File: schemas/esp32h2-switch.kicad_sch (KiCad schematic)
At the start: 37 parts, among them J1 Screw_Terminal_01x02, J2 Conn_01x15, J3 Screw_Terminal_01x02, K1 SPDT, 5V 72R, 10A 250VAC, Q1 NPN, 40V, 500mA, T1 1:1 330uH / 15uH, U1 LM1117MP-3.3, U2 LNK306P, U3 PC817

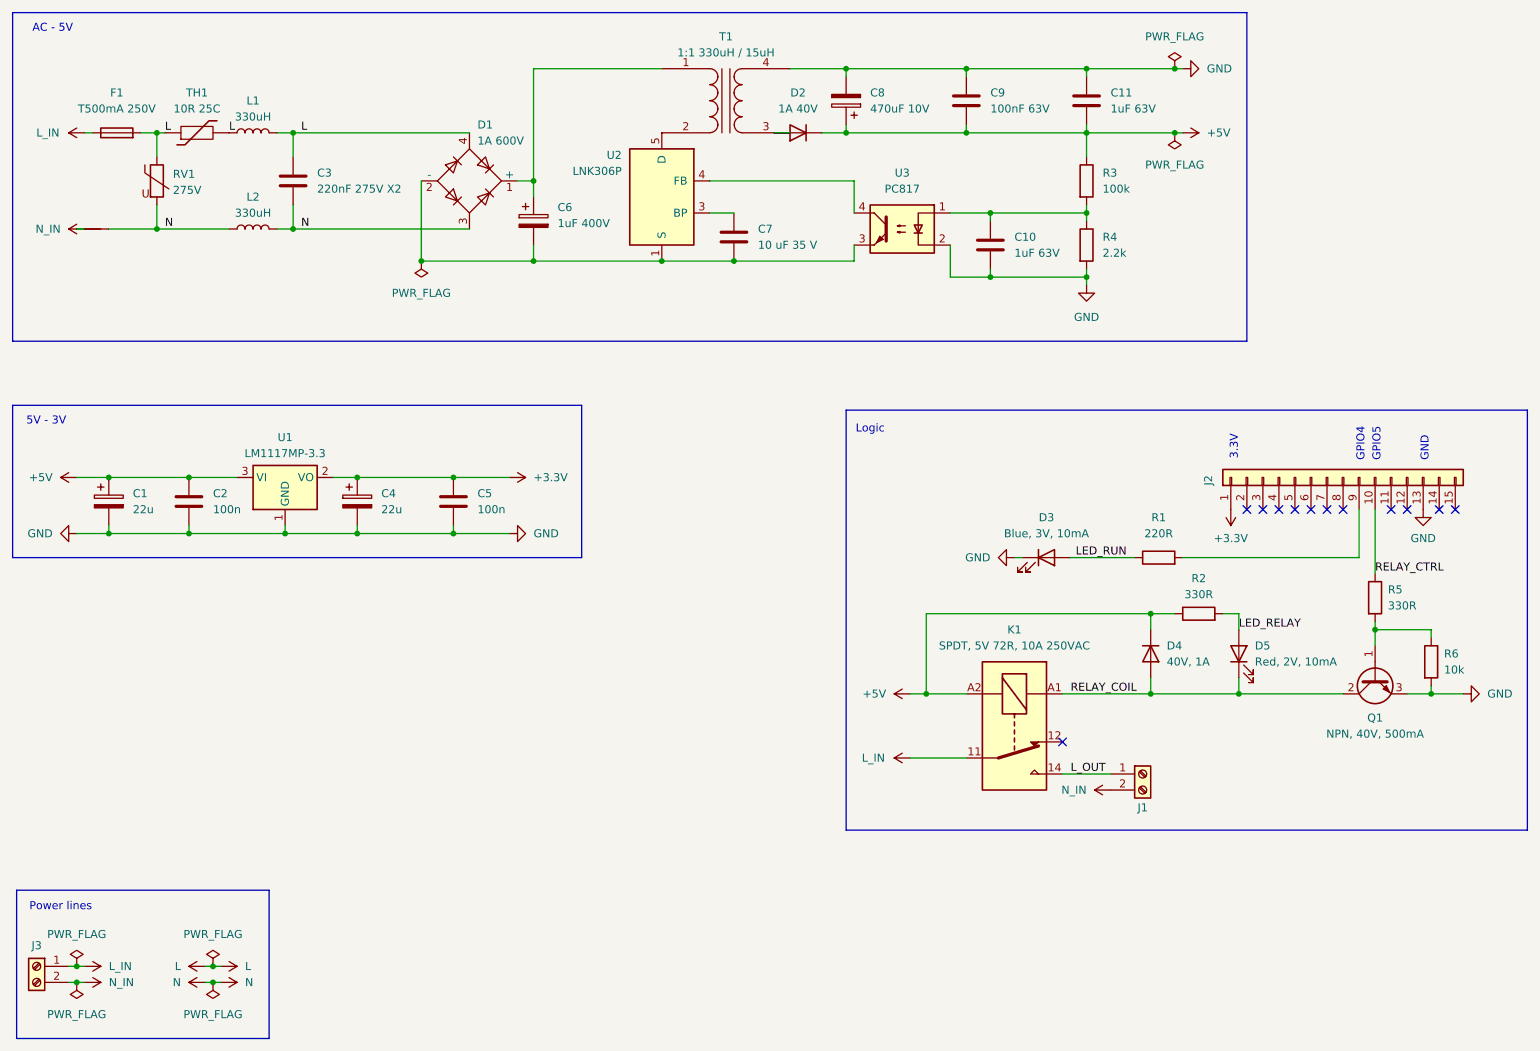
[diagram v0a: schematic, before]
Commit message: Improve layout a lot
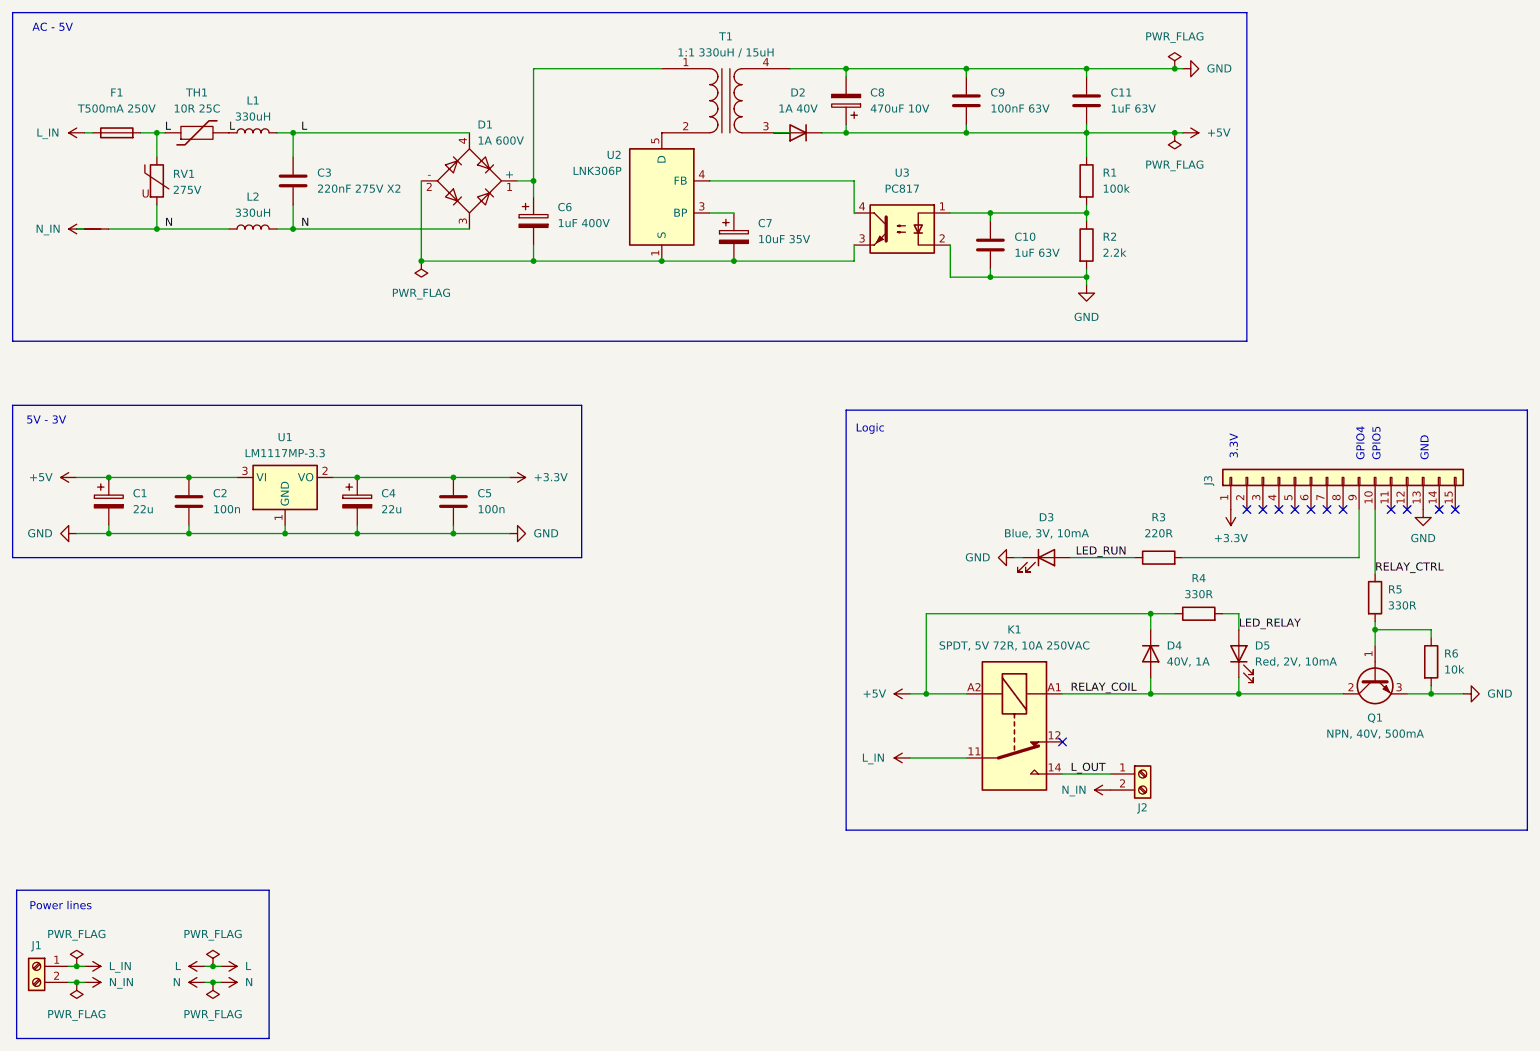
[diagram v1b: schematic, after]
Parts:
- removed C7: 10 uF 35 V, symbol Device:C
- added C7: 10uF 35V, Capacitor_THT:CP_Radial_Tantal_D6.0mm_P2.50mm, symbol Device:C_Polarized
- C10, C11: footprint (none) -> Capacitor_THT:C_Disc_D4.3mm_W1.9mm_P5.00mm
- C3: footprint (none) -> Capacitor_THT:C_Rect_L26.5mm_W5.0mm_P22.50mm_MKS4
- C6, C8: footprint (none) -> Capacitor_THT:CP_Radial_D6.3mm_P2.50mm
- C9: footprint (none) -> Capacitor_THT:C_Disc_D6.0mm_W2.5mm_P5.00mm
- D2: footprint (none) -> Diode_THT:D_DO-41_SOD81_P10.16mm_Horizontal
- J2: renamed from J1; footprint TerminalBlock_Phoenix:TerminalBlock_Phoenix_MKDS-1,5-2-5.08_1x02_P5.08mm_Horizontal -> Connector_PinSocket_2.54mm:PinSocket_1x15_P2.54mm_Vertical
- J3: renamed from J2; footprint Connector_PinSocket_2.54mm:PinSocket_1x15_P2.54mm_Vertical -> TerminalBlock_Phoenix:TerminalBlock_Phoenix_MKDS-1,5-2-5.08_1x02_P5.08mm_Horizontal
- L1, L2: footprint (none) -> Inductor_THT:L_Toroid_Vertical_L24.6mm_W15.5mm_P11.44mm_Pulse_KM-4
- R1: renamed from R3; footprint (none) -> Resistor_THT:R_Axial_DIN0207_L6.3mm_D2.5mm_P7.62mm_Horizontal
- R2: renamed from R4; footprint (none) -> Resistor_THT:R_Axial_DIN0207_L6.3mm_D2.5mm_P7.62mm_Horizontal
- renumbered J3 to J1, R1 to R3, R2 to R4
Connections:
- net at U2.3 (BP): now also C7.1
- net at C6.2, D1.2 (-), U2.1 (S)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: now also C7.2
